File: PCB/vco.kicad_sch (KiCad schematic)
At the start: 17 parts, among them J5 VCO, Q3 2N3904, Q4 2N3904, U1 LM324

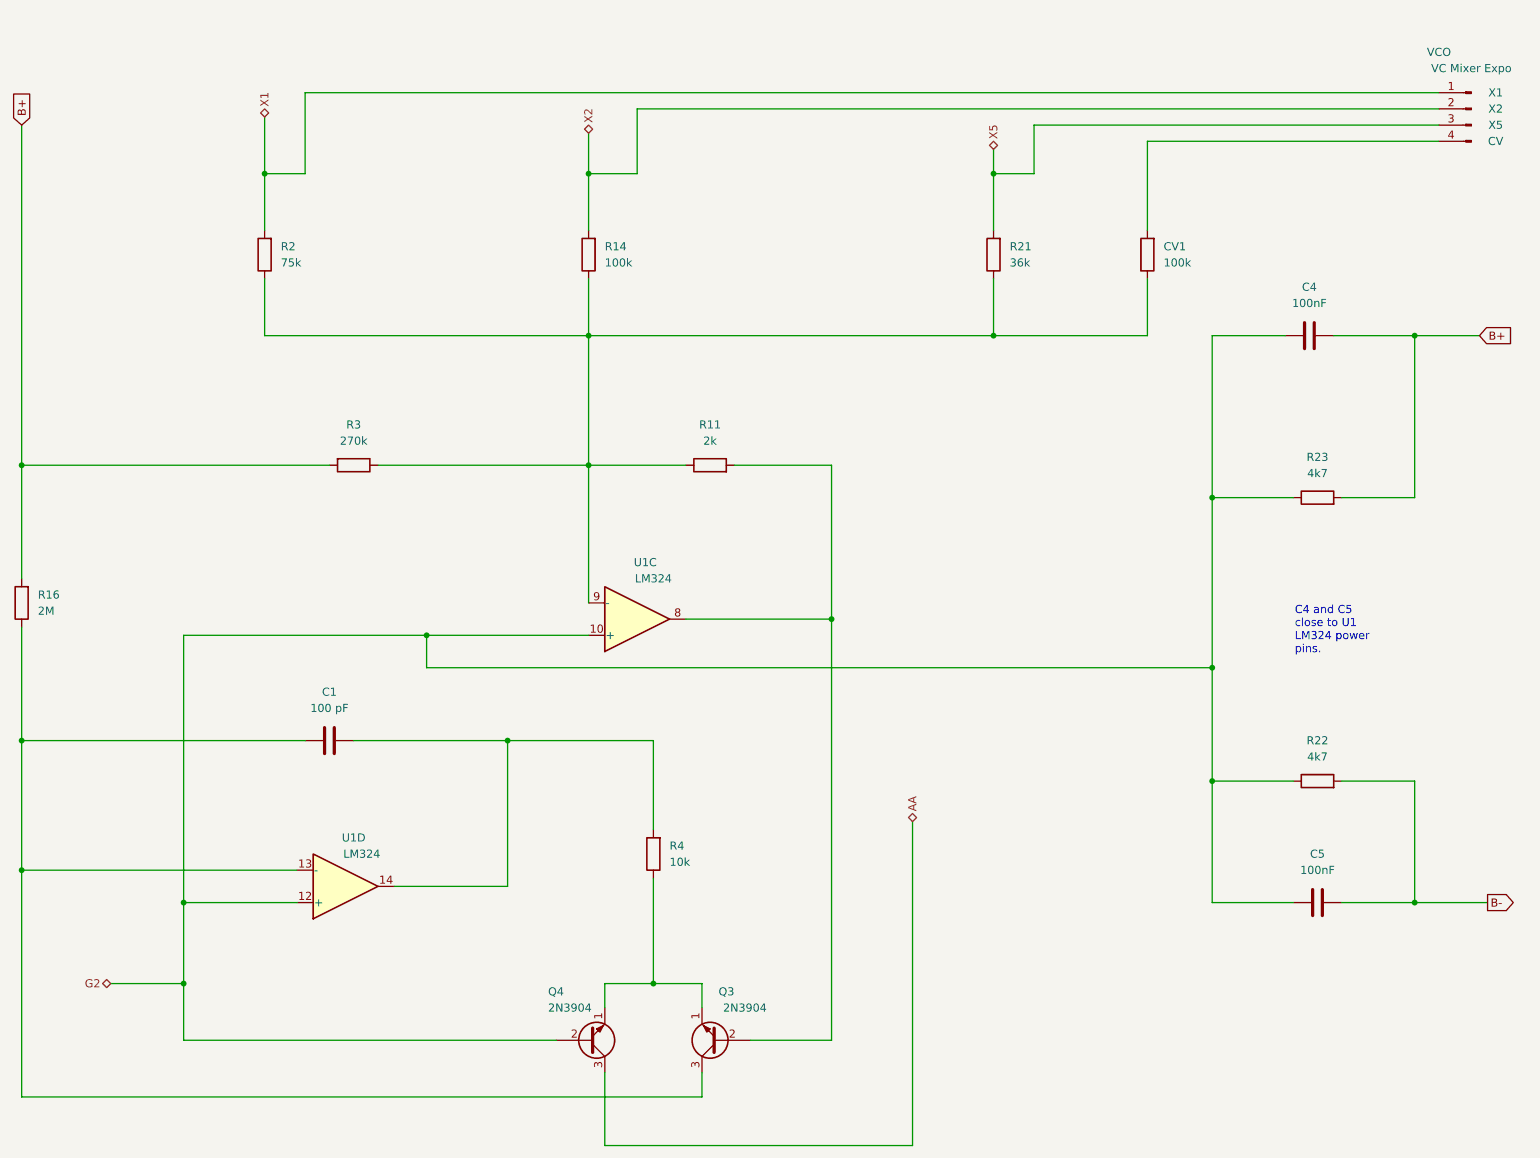
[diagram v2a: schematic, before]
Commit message: Final Update
Move power pins closer to filter caps
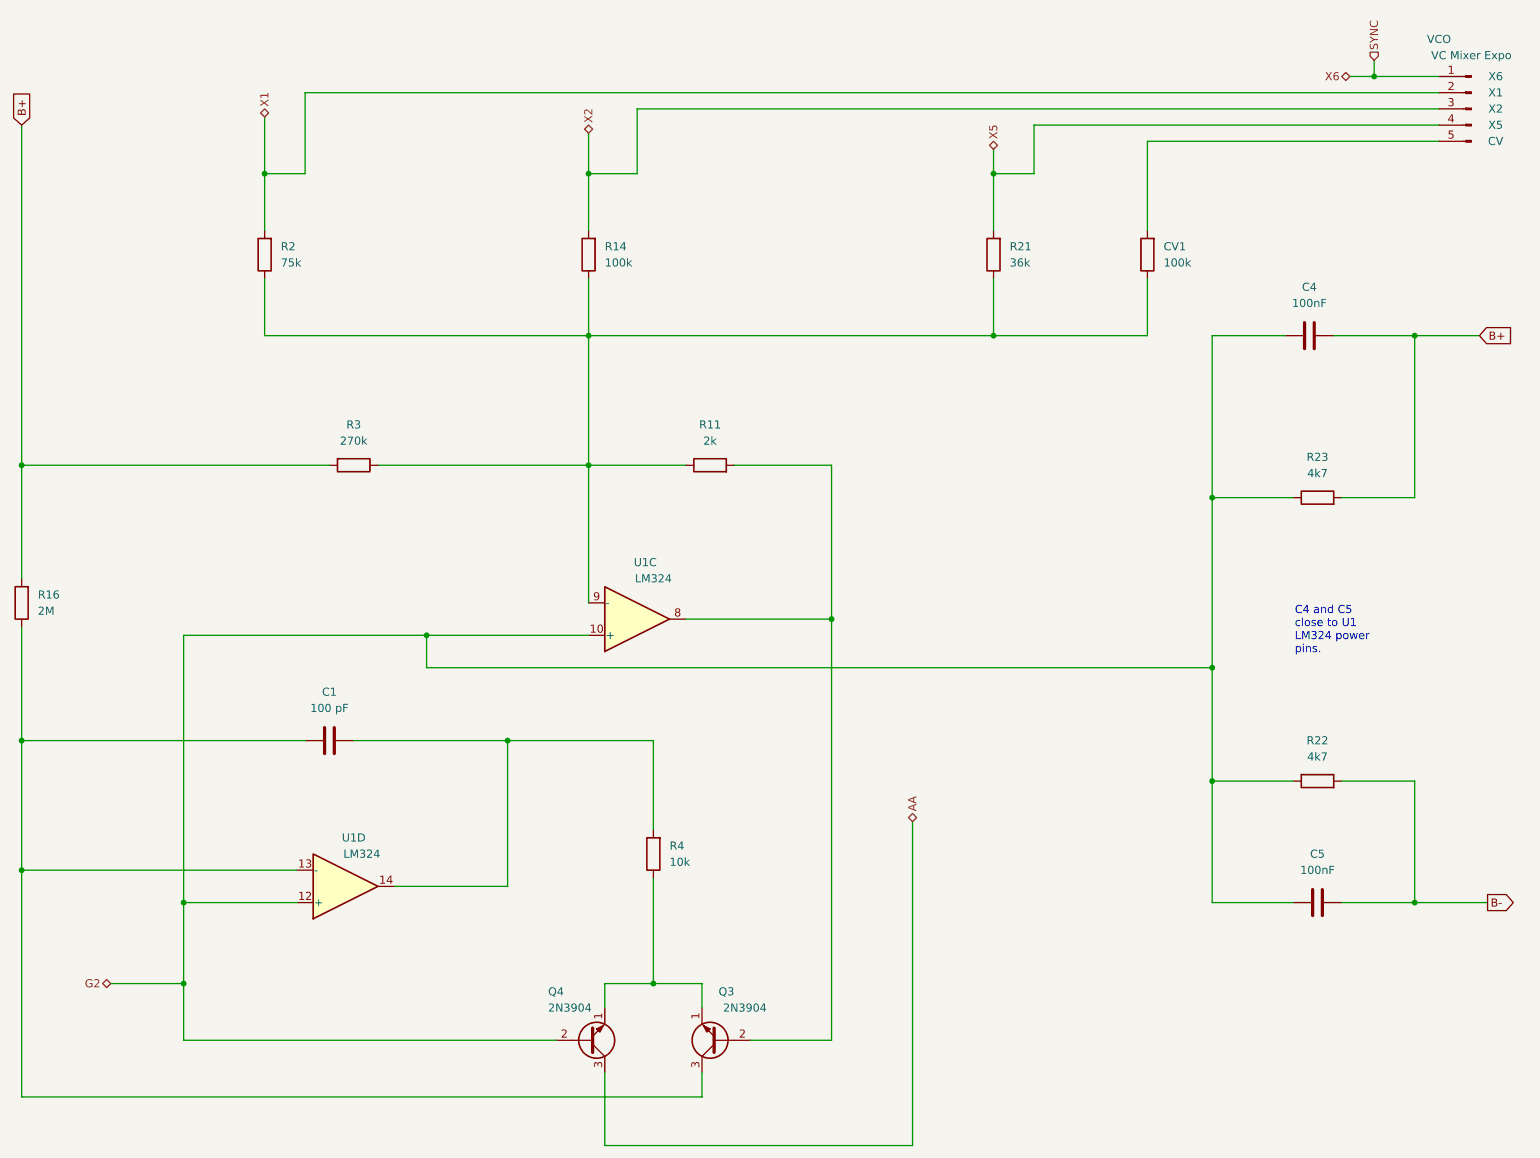
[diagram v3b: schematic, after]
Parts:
- J5: footprint Connector_PinSocket_2.54mm:PinSocket_1x04_P2.54mm_Vertical -> Connector_PinSocket_2.54mm:PinSocket_1x05_P2.54mm_Vertical; symbol Connector:Conn_01x04_Pin -> Connector:Conn_01x05_Pin; X6 (none) -> X6
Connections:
- net X1: now also J5.2 (Pin_2); no longer J5.1 (Pin_1)
- net X2: now also J5.3 (Pin_3); no longer J5.2 (Pin_2)
- net X5: now also J5.4 (Pin_4); no longer J5.3 (Pin_3)
- net at CV1.2: now also J5.5 (Pin_5); no longer J5.4 (Pin_4)
- new net SYNC: J5.1 (Pin_1)
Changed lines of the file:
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@@
+	)
+	(junction
+		(at 237.49 22.86)
+		(diameter 0)
+		(color 0 0 0 0)
 	)
 	(junction
@@
 	(wire
 		(pts
+			(xy 237.49 20.32) (xy 237.49 22.86)
+		)
+		(stroke
+			(width 0)
+			(type default)
+		)
+	)
+	(wire
+		(pts
 			(xy 137.16 83.82) (xy 152.4 83.82)
 		)
@@
 	(wire
 		(pts
+			(xy 237.49 22.86) (xy 233.68 22.86)
+		)
+		(stroke
+			(width 0)
+			(type default)
+		)
+	)
+	(wire
+		(pts
 			(xy 88.9 110.49) (xy 88.9 115.57)
 		)
@@
 		(pts
 			(xy 121.92 27.94) (xy 121.92 38.1)
+		)
+		(stroke
+			(width 0)
+			(type default)
+		)
+	)
+	(wire
+		(pts
+			(xy 247.65 22.86) (xy 237.49 22.86)
 		)
 		(stroke
@@
 		)
 	)
+	(hierarchical_label "SYNC"
+		(shape input)
+		(at 237.49 20.32 90)
+		(effects
+			(font
+				(size 1.27 1.27)
+			)
+			(justify left)
+		)
+	)
 	(hierarchical_label "X1"
 		(shape bidirectional)
@@
 			)
 			(justify left)
+		)
+	)
+	(hierarchical_label "X6"
+		(shape bidirectional)
+		(at 233.68 22.86 180)
+		(effects
+			(font
+				(size 1.27 1.27)
+			)
+			(justify right)
 		)
 	)
@@
 			)
 		)
-		(property "Description" ""
+		(property "Description" "0.2A Ic, 40V Vce, Small Signal NPN Transistor, TO-92"
+			(at 134.62 173.99 0)
+			(hide yes)
+			(show_name no)
+			(do_not_autoplace no)
+			(effects
+				(font
+					(size 1.27 1.27)
+				)
+			)
+		)
+		(property "Sim.Device" "NPN"
+			(at 134.62 173.99 0)
+			(hide yes)
+			(show_name no)
+			(do_not_autoplace no)
+			(effects
+				(font
+					(size 1.27 1.27)
+				)
+			)
+		)
+		(property "Sim.Pins" "1=E 2=B 3=C"
 			(at 134.62 173.99 0)
 			(hide yes)
@@
 	)
 	(symbol
-		(lib_id "Connector:Conn_01x04_Pin")
+		(lib_id "Connector:Conn_01x05_Pin")
 		(at 252.73 27.94 0)
 		(mirror y)
@@
 		)
 		(property "Value" "VCO"
-			(at 247.65 19.05 0)
-			(show_name no)
-			(do_not_autoplace no)
-			(effects
-				(font
-					(size 1.27 1.27)
-				)
-			)
-		)
-		(property "Footprint" "Connector_PinSocket_2.54mm:PinSocket_1x04_P2.54mm_Vertical"
+			(at 247.65 17.018 0)
+			(show_name no)
+			(do_not_autoplace no)
+			(effects
+				(font
+					(size 1.27 1.27)
+				)
+			)
+		)
+		(property "Footprint" "Connector_PinSocket_2.54mm:PinSocket_1x05_P2.54mm_Vertical"
 			(at 252.73 27.94 0)
 			(hide yes)
@@
 			)
 		)
-		(property "Description" "Generic connector, single row, 01x04, script generated"
+		(property "Description" "Generic connector, single row, 01x05, script generated"
 			(at 252.73 27.94 0)
 			(hide yes)
@@
 		)
 		(property "Wert2" "VC Mixer Expo"
-			(at 252.73 21.59 0)
+			(at 252.73 19.558 0)
 			(show_name no)
 			(do_not_autoplace no)
@@
 			)
 		)
+		(property "X6" "X6"
+			(at 256.54 22.86 0)
+			(show_name no)
+			(do_not_autoplace no)
+			(effects
+				(font
+					(size 1.27 1.27)
+				)
+			)
+		)
 		(pin "1"
 		)
@@
 		)
 		(pin "4"
+		)
+		(pin "5"
 		)
 		(instances
@@
 			)
 		)
-		(property "Description" ""
+		(property "Description" "0.2A Ic, 40V Vce, Small Signal NPN Transistor, TO-92"
 			(at 114.3 173.99 0)
 			(hide yes)
+			(show_name no)
+			(do_not_autoplace no)
+			(effects
+				(font
+					(size 1.27 1.27)
+				)
+			)
+		)
+		(property "Sim.Device" "NPN"
+			(at 114.3 173.99 0)
+			(hide yes)
+			(show_name no)
+			(do_not_autoplace no)
+			(effects
+				(font
+					(size 1.27 1.27)
+				)
+			)
+		)
+		(property "Sim.Pins" "1=E 2=B 3=C"
+			(at 114.3 173.99 0)
+			(hide yes)
